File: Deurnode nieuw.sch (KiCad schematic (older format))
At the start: 34 parts, among them J1 EXT1, J12 Screw_Terminal_01x03, J14 Screw_Terminal_01x02, J15 Screw_Terminal_01x02, J18 BarrelJack_DC5.5F, J19 Jumper Use external 12V, J2 EXT2, J22 Force output Rel./FET on, J3 Conn_01x08, J4 Screw_Terminal_01x03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

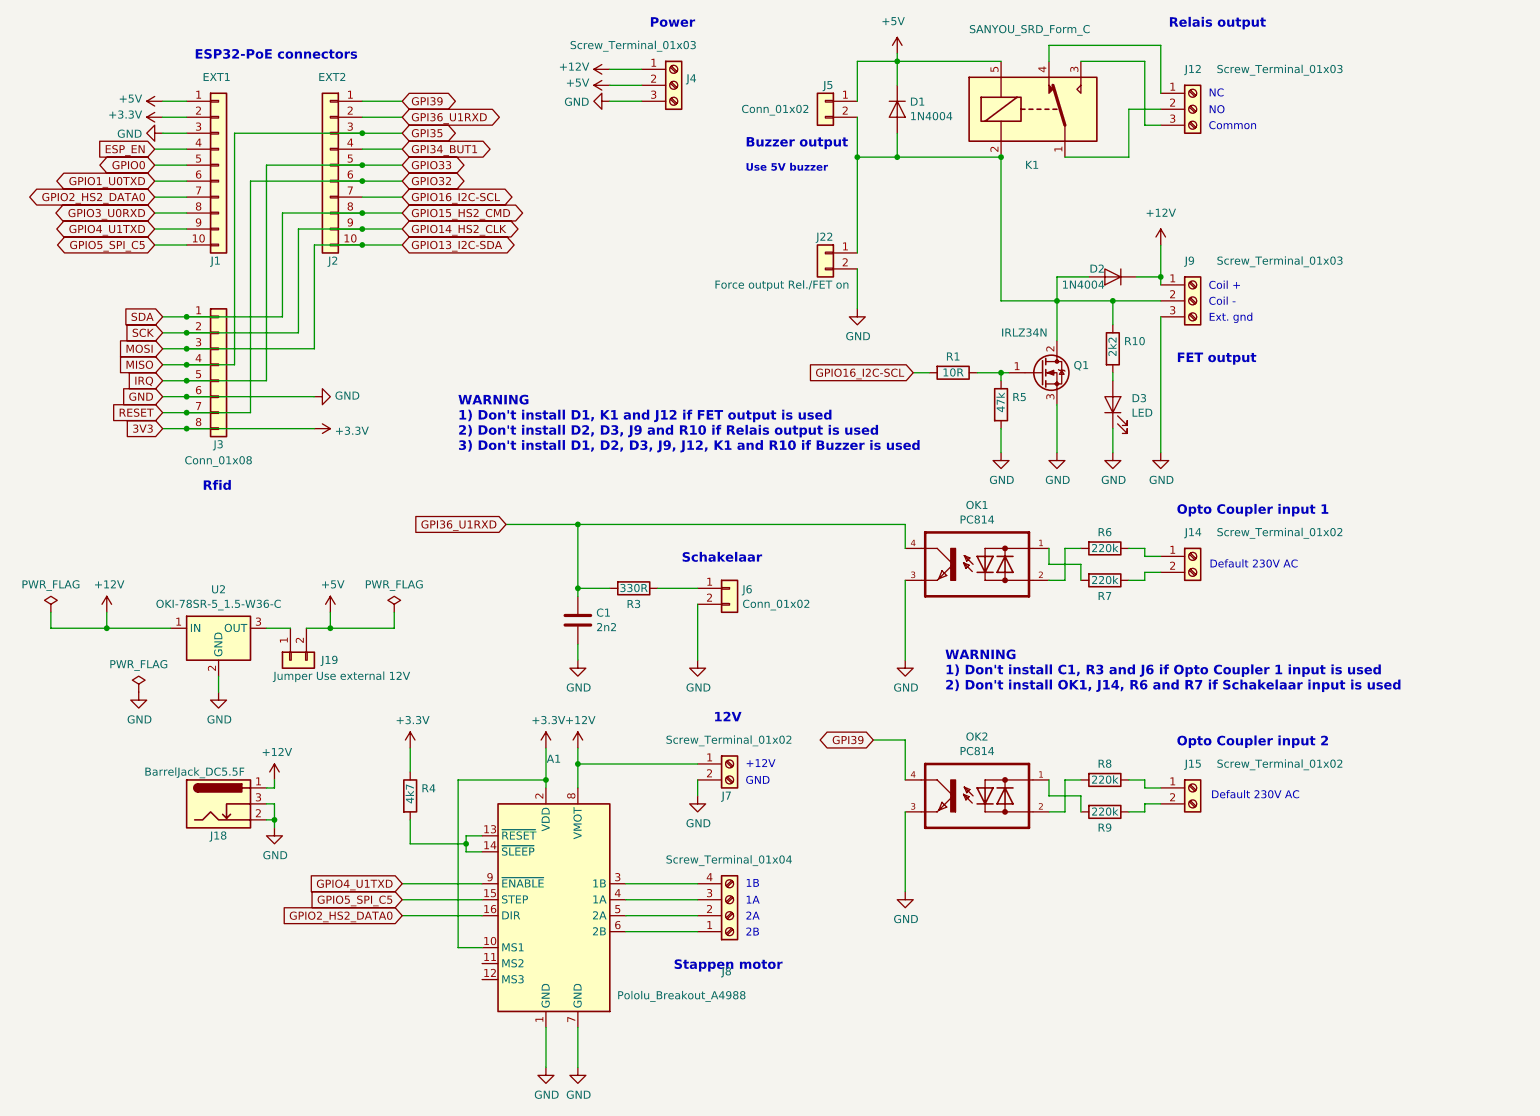
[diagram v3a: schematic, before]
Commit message: Relais and FET are controlled separately, buzzer resistor added. Current version Concep V0.8
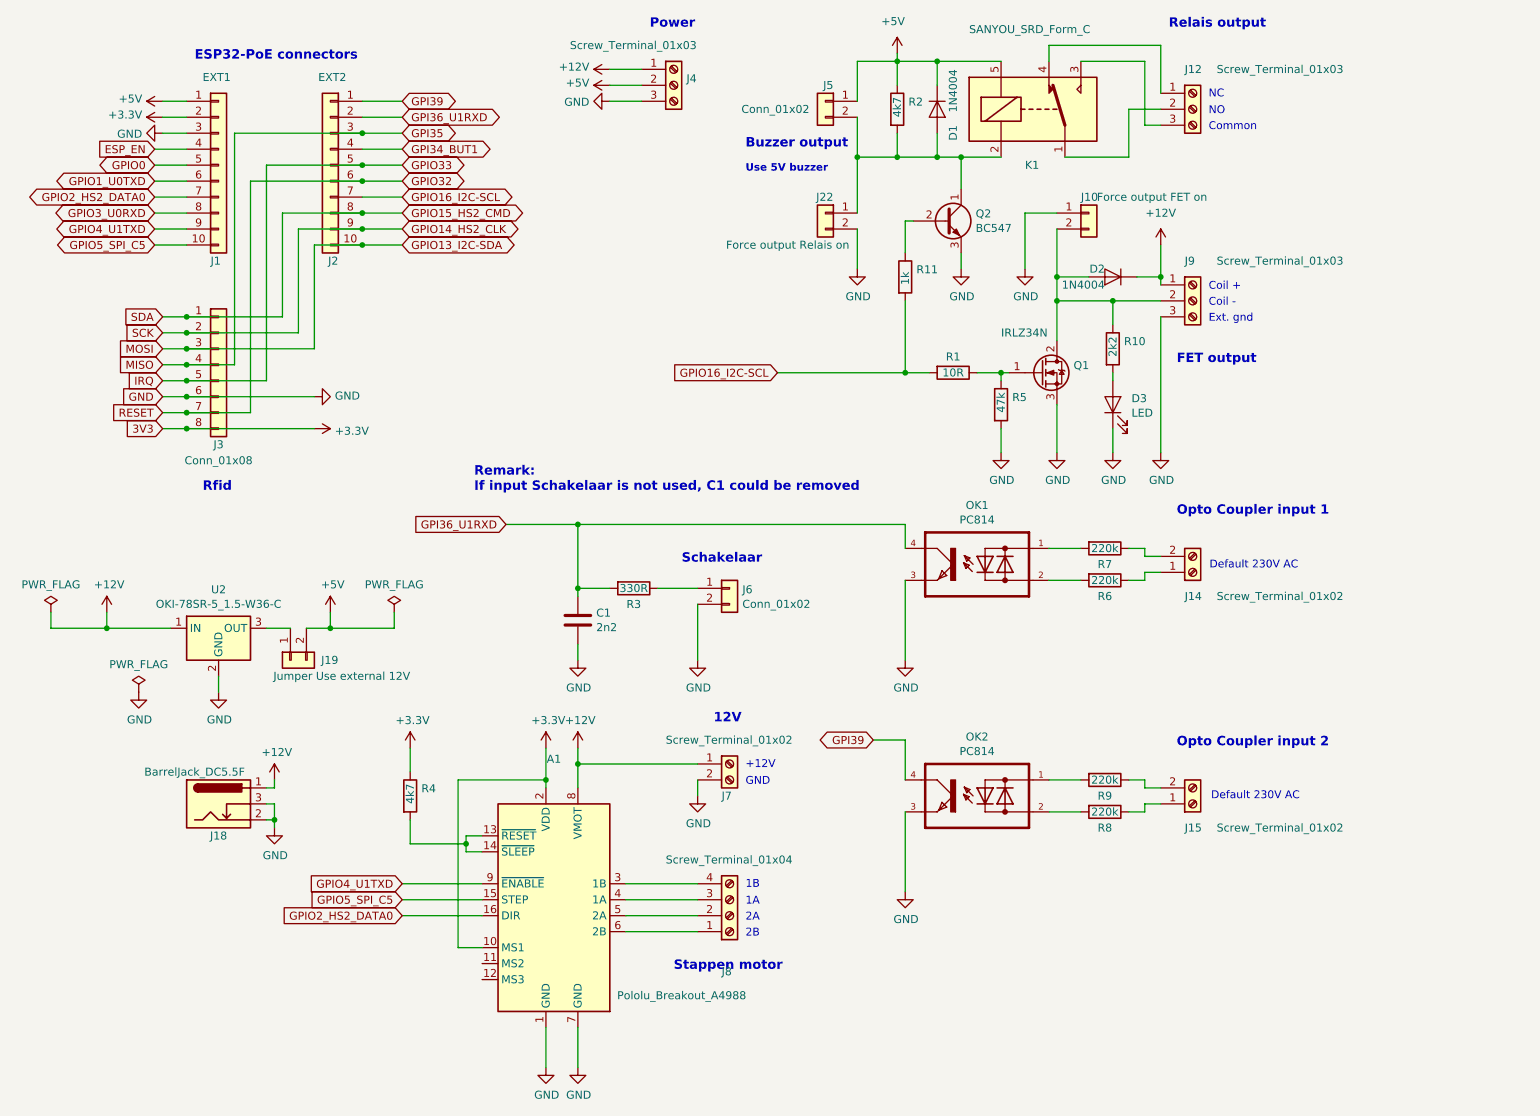
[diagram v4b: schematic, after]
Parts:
- added J10: Force output FET on, Connector_PinHeader_2.54mm:PinHeader_1x02_P2.54mm_Vertical, symbol Connector_Generic:Conn_01x02
- added Q2: BC547, Package_TO_SOT_THT:TO-92_Inline, symbol Transistor_BJT:BC547
- added R11: 1k, Resistor_THT:R_Axial_DIN0207_L6.3mm_D2.5mm_P7.62mm_Horizontal, symbol Device:R
- added R2: 4k7, Resistor_THT:R_Axial_DIN0207_L6.3mm_D2.5mm_P7.62mm_Horizontal, symbol Device:R
- J22: value Force output Rel./FET on -> Force output Relais on
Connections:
- net +5V: now also R2.1
- net GND: now also J10.1 (Pin_1), Q2.3 (E)
- net GPIO16_I2C-SCL: now also R11.2
- net at D1.2 (A), J22.1 (Pin_1), J5.2 (Pin_2)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: now also Q2.1 (C), R2.2; no longer D2.2 (A), J9.2 (Pin_2), Q1.2 (D), R10.1
- new net: D2.2 (A), J10.2 (Pin_2), J9.2 (Pin_2), Q1.2 (D), R10.1
- new net: Q2.2 (B), R11.1
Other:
- note added: "Remark:\nIf input Schakelaar is not used, C1 could be removed"
- note removed: "WARNING\n1) Don't install C1, R3 and J6 if Opto Coupler 1 input is used\n2) Don't install OK1, J14, R6 and R7 if Schakelaar input is used"
- note removed: "WARNING\n1) Don't install D1, K1 and J12 if FET output is used\n2) Don't install D2, D3, J9 and R10 if Relais output is used\n3) Don't install D1, D2, D3, J9, J12, K1 and R10 if Buzzer is used"
- moved on the sheet: D1, J22, R6, R7, R8, R9
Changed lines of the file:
@@
 Sheet 1 1
 Title "Deurnode (based on Olimex ESP32-POE)"
-Date "2020-03-07"
-Rev "Version 0.7"
+Date "2020-03-08"
+Rev "Version 0.8"
 Comp "Makerspace Leiden"
 Comment1 "Hans Beerman"
@@
 	0    1    1    0
 $EndComp
-Text GLabel 6850 2800 0    50   Input ~ 0
+Text GLabel 6000 2800 0    50   Input ~ 0
 GPIO16_I2C-SCL
 Wire Wire Line
@@
 Wire Wire Line
 	6750 1000 6750 850
-Wire Wire Line
-	6750 850  7400 850
 $Comp
 L power:+5V #PWR04
@@
 L Connector:Screw_Terminal_01x02 J14
 U 1 1 5E5F8709
-P 8600 3950
-F 0 "J14" H 8550 4100 50  0000 L CNN
-F 1 "Screw_Terminal_01x02" H 8750 4100 50  0000 L CNN
-F 2 "TerminalBlock_RND:TerminalBlock_RND_205-00287_1x02_P5.08mm_Horizontal" H 8600 3950 50  0001 C CNN
-F 3 "~" H 8600 3950 50  0001 C CNN
-	1    8600 3950
-	1    0    0    -1
+P 8600 4050
+F 0 "J14" H 8550 4200 50  0000 L CNN
+F 1 "Screw_Terminal_01x02" H 8750 4200 50  0000 L CNN
+F 2 "TerminalBlock_RND:TerminalBlock_RND_205-00287_1x02_P5.08mm_Horizontal" H 8600 4050 50  0001 C CNN
+F 3 "~" H 8600 4050 50  0001 C CNN
+	1    8600 4050
+	1    0    0    1
 $EndComp
 $Comp
 L Device:R R6
 U 1 1 5E5F9735
-P 8050 3900
-F 0 "R6" V 7950 3900 50  0000 C CNN
-F 1 "220k" V 8050 3900 50  0000 C CNN
-F 2 "Resistor_THT:R_Axial_DIN0207_L6.3mm_D2.5mm_P7.62mm_Horizontal" V 7980 3900 50  0001 C CNN
-F 3 "~" H 8050 3900 50  0001 C CNN
-	1    8050 3900
-	0    1    1    0
-$EndComp
-$Comp
-L Device:R R7
-U 1 1 5E5F9EE9
 P 8050 4100
-F 0 "R7" V 8150 4100 50  0000 C CNN
+F 0 "R6" V 8150 4100 50  0000 C CNN
 F 1 "220k" V 8050 4100 50  0000 C CNN
 F 2 "Resistor_THT:R_Axial_DIN0207_L6.3mm_D2.5mm_P7.62mm_Horizontal" V 7980 4100 50  0001 C CNN
@@
 L Connector:Screw_Terminal_01x02 J15
 U 1 1 5E676B21
-P 8600 5400
-F 0 "J15" H 8550 5550 50  0000 L CNN
-F 1 "Screw_Terminal_01x02" H 8750 5550 50  0000 L CNN
-F 2 "TerminalBlock_RND:TerminalBlock_RND_205-00287_1x02_P5.08mm_Horizontal" H 8600 5400 50  0001 C CNN
-F 3 "~" H 8600 5400 50  0001 C CNN
-	1    8600 5400
-	1    0    0    -1
+P 8600 5500
+F 0 "J15" H 8550 5650 50  0000 L CNN
+F 1 "Screw_Terminal_01x02" H 8750 5650 50  0000 L CNN
+F 2 "TerminalBlock_RND:TerminalBlock_RND_205-00287_1x02_P5.08mm_Horizontal" H 8600 5500 50  0001 C CNN
+F 3 "~" H 8600 5500 50  0001 C CNN
+	1    8600 5500
+	1    0    0    1
 $EndComp
 $Comp
 L Device:R R8
 U 1 1 5E676B27
+P 8050 5550
+F 0 "R8" V 8150 5550 50  0000 C CNN
+F 1 "220k" V 8050 5550 50  0000 C CNN
+F 2 "Resistor_THT:R_Axial_DIN0207_L6.3mm_D2.5mm_P7.62mm_Horizontal" V 7980 5550 50  0001 C CNN
+F 3 "~" H 8050 5550 50  0001 C CNN
+	1    8050 5550
+	0    1    1    0
+$EndComp
+$Comp
+L Device:R R9
+U 1 1 5E676B2D
 P 8050 5350
-F 0 "R8" V 7950 5350 50  0000 C CNN
+F 0 "R9" V 8150 5350 50  0000 C CNN
 F 1 "220k" V 8050 5350 50  0000 C CNN
 F 2 "Resistor_THT:R_Axial_DIN0207_L6.3mm_D2.5mm_P7.62mm_Horizontal" V 7980 5350 50  0001 C CNN
 F 3 "~" H 8050 5350 50  0001 C CNN
 	1    8050 5350
-	0    1    1    0
-$EndComp
-$Comp
-L Device:R R9
-U 1 1 5E676B2D
-P 8050 5550
-F 0 "R9" V 8150 5550 50  0000 C CNN
-F 1 "220k" V 8050 5550 50  0000 C CNN
-F 2 "Resistor_THT:R_Axial_DIN0207_L6.3mm_D2.5mm_P7.62mm_Horizontal" V 7980 5550 50  0001 C CNN
-F 3 "~" H 8050 5550 50  0001 C CNN
-	1    8050 5550
 	0    1    1    0
 $EndComp
@@
 Text Notes 8715 5480 0    49   ~ 0
 Default 230V AC
-Wire Wire Line
-	6950 2800 6850 2800
 $Comp
 L power:GND #PWR0110
 U 1 1 5E6923E9
-P 6500 2400
-F 0 "#PWR0110" H 6500 2150 50  0001 C CNN
-F 1 "GND" H 6505 2227 50  0000 C CNN
-F 2 "" H 6500 2400 50  0001 C CNN
-F 3 "" H 6500 2400 50  0001 C CNN
-	1    6500 2400
-	1    0    0    -1
-$EndComp
-Wire Wire Line
-	6500 2400 6500 2150
+P 6500 2150
+F 0 "#PWR0110" H 6500 1900 50  0001 C CNN
+F 1 "GND" H 6505 1977 50  0000 C CNN
+F 2 "" H 6500 2150 50  0001 C CNN
+F 3 "" H 6500 2150 50  0001 C CNN
+	1    6500 2150
+	1    0    0    -1
+$EndComp
+Wire Wire Line
+	6500 2150 6500 1900
 $Comp
 L Connector:Barrel_Jack_Switch J18
@@
 L Connector_Generic:Conn_01x02 J22
 U 1 1 5E6404FC
-P 6300 2050
-F 0 "J22" H 6250 2150 50  0000 L CNN
-F 1 "Force output Rel./FET on" H 6150 1850 50  0000 L CNN
-F 2 "Connector_PinHeader_2.54mm:PinHeader_1x02_P2.54mm_Vertical" H 6300 2050 50  0001 C CNN
-F 3 "~" H 6300 2050 50  0001 C CNN
-	1    6300 2050
+P 6300 1800
+F 0 "J22" H 6250 1900 50  0000 L CNN
+F 1 "Force output Relais on" H 6150 1600 50  0000 L CNN
+F 2 "Connector_PinHeader_2.54mm:PinHeader_1x02_P2.54mm_Vertical" H 6300 1800 50  0001 C CNN
+F 3 "~" H 6300 1800 50  0001 C CNN
+	1    6300 1800
 	-1   0    0    -1
 $EndComp
-Wire Wire Line
-	7400 1450 7400 2350
-Wire Wire Line
-	7400 2350 7750 2350
 $Comp
 L power:+12V #PWR016
@@
 Wire Wire Line
 	8400 2200 8400 2250
-Text Notes 4000 3300 0    59   ~ 12
-WARNING\n1) Don't install D1, K1 and J12 if FET output is used\n2) Don't install D2, D3, J9 and R10 if Relais output is used\n3) Don't install D1, D2, D3, J9, J12, K1 and R10 if Buzzer is used
 Wire Wire Line
 	7250 2800 7400 2800
@@
 L Diode:1N4004 D1
 U 1 1 5E593BB3
-P 6750 1150
-F 0 "D1" V 6704 1229 50  0000 L CNN
-F 1 "1N4004" V 6795 1229 50  0000 L CNN
-F 2 "Diode_THT:D_DO-41_SOD81_P10.16mm_Horizontal" H 6750 975 50  0001 C CNN
-F 3 "http://www.vishay.com/docs/88503/1n4001.pdf" H 6750 1150 50  0001 C CNN
-	1    6750 1150
+P 7000 1150
+F 0 "D1" H 7100 1250 50  0000 L CNN
+F 1 "1N4004" H 6750 1250 50  0000 L CNN
+F 2 "Diode_THT:D_DO-41_SOD81_P10.16mm_Horizontal" H 7000 975 50  0001 C CNN
+F 3 "http://www.vishay.com/docs/88503/1n4001.pdf" H 7000 1150 50  0001 C CNN
+	1    7000 1150
 	0    1    1    0
 $EndComp
@@
 Connection ~ 6750 1450
 Wire Wire Line
-	6750 1450 7400 1450
-Wire Wire Line
-	6500 2050 6500 1450
+	6500 1800 6500 1450
 Connection ~ 6500 1450
-Text Notes 7050 4800 0    59   ~ 12
-WARNING\n1) Don't install C1, R3 and J6 if Opto Coupler 1 input is used\n2) Don't install OK1, J14, R6 and R7 if Schakelaar input is used
+Text Notes 4100 3550 0    59   ~ 12
+Remark:\nIf input Schakelaar is not used, C1 could be removed
 Wire Wire Line
 	7800 1450 8200 1450
@@
 	1    0    0    -1
 $EndComp
-Connection ~ 7400 1450
-Wire Wire Line
-	7700 4100 7800 4100
-Wire Wire Line
-	7800 4100 7800 3900
-Wire Wire Line
-	7800 3900 7900 3900
-Wire Wire Line
-	7900 4100 7900 4000
-Wire Wire Line
-	7900 4000 7700 4000
-Wire Wire Line
-	7700 4000 7700 3900
-Wire Wire Line
-	7700 5350 7700 5450
-Wire Wire Line
-	7700 5450 7900 5450
-Wire Wire Line
-	7900 5450 7900 5550
-Wire Wire Line
-	7700 5550 7800 5550
-Wire Wire Line
-	7800 5550 7800 5350
-Wire Wire Line
-	7800 5350 7900 5350
+$Comp
+L Transistor_BJT:BC547 Q2
+U 1 1 5E6740A8
+P 7050 1850
+F 0 "Q2" H 7241 1896 50  0000 L CNN
+F 1 "BC547" H 7241 1805 50  0000 L CNN
+F 2 "Package_TO_SOT_THT:TO-92_Inline" H 7250 1775 50  0001 L CIN
+F 3 "http://www.fairchildsemi.com/ds/BC/BC547.pdf" H 7050 1850 50  0001 L CNN
+	1    7050 1850
+	1    0    0    -1
+$EndComp
+$Comp
+L power:GND #PWR011
+U 1 1 5E67C879
+P 7150 2150
+F 0 "#PWR011" H 7150 1900 50  0001 C CNN
+F 1 "GND" H 7155 1977 50  0000 C CNN
+F 2 "" H 7150 2150 50  0001 C CNN
+F 3 "" H 7150 2150 50  0001 C CNN
+	1    7150 2150
+	1    0    0    -1
+$EndComp
+Wire Wire Line
+	7150 2150 7150 2050
+Wire Wire Line
+	6950 2800 6800 2800
+$Comp
+L Device:R R11
+U 1 1 5E68BC49
+P 6800 2200
+F 0 "R11" H 6870 2246 50  0000 L CNN
+F 1 "1k" V 6800 2150 50  0000 L CNN
+F 2 "Resistor_THT:R_Axial_DIN0207_L6.3mm_D2.5mm_P7.62mm_Horizontal" V 6730 2200 50  0001 C CNN
+F 3 "~" H 6800 2200 50  0001 C CNN
+	1    6800 2200
+	1    0    0    -1
+$EndComp
+Wire Wire Line
+	6800 2350 6800 2800
+Connection ~ 6800 2800
+Wire Wire Line
+	6800 2800 6000 2800
+Wire Wire Line
+	6800 2050 6800 1850
+Wire Wire Line
+	6800 1850 6850 1850
+$Comp
+L Connector_Generic:Conn_01x02 J10
+U 1 1 5E6B22A0
+P 7950 1800
+F 0 "J10" H 7900 1900 50  0000 L CNN
+F 1 "Force output FET on" H 8000 1900 50  0000 L CNN
+F 2 "Connector_PinHeader_2.54mm:PinHeader_1x02_P2.54mm_Vertical" H 7950 1800 50  0001 C CNN
+F 3 "~" H 7950 1800 50  0001 C CNN
+	1    7950 1800
+	1    0    0    -1
+$EndComp
+Wire Wire Line
+	7150 1650 7150 1450
+Connection ~ 7150 1450
+Wire Wire Line
+	7150 1450 7400 1450
+Wire Wire Line
+	7750 1900 7750 2200
+Connection ~ 7750 2200
+$Comp
+L power:GND #PWR018
+U 1 1 5E6DA6A3
+P 7550 2150
+F 0 "#PWR018" H 7550 1900 50  0001 C CNN
+F 1 "GND" H 7555 1977 50  0000 C CNN
+F 2 "" H 7550 2150 50  0001 C CNN
+F 3 "" H 7550 2150 50  0001 C CNN
+	1    7550 2150
+	1    0    0    -1
+$EndComp
+Wire Wire Line
+	7550 2150 7550 1800
+Wire Wire Line
+	7550 1800 7750 1800
+Wire Wire Line
+	6750 850  7000 850
+Wire Wire Line
+	6750 1450 7000 1450
+Wire Wire Line
+	7000 1300 7000 1450
+Connection ~ 7000 1450
+Wire Wire Line
+	7000 1450 7150 1450
+Wire Wire Line
+	7000 1000 7000 850
+Connection ~ 7000 850
+Wire Wire Line
+	7000 850  7400 850
+$Comp
+L Device:R R2
+U 1 1 5E705D16
+P 6750 1150
+F 0 "R2" H 6820 1196 50  0000 L CNN
+F 1 "4k7" V 6750 1100 50  0000 L CNN
+F 2 "Resistor_THT:R_Axial_DIN0207_L6.3mm_D2.5mm_P7.62mm_Horizontal" V 6680 1150 50  0001 C CNN
+F 3 "~" H 6750 1150 50  0001 C CNN
+	1    6750 1150
+	1    0    0    -1
+$EndComp
+$Comp
+L Device:R R7
+U 1 1 5E5F9EE9
+P 8050 3900
+F 0 "R7" V 8150 3900 50  0000 C CNN
+F 1 "220k" V 8050 3900 50  0000 C CNN
+F 2 "Resistor_THT:R_Axial_DIN0207_L6.3mm_D2.5mm_P7.62mm_Horizontal" V 7980 3900 50  0001 C CNN
+F 3 "~" H 8050 3900 50  0001 C CNN
+	1    8050 3900
+	0    1    1    0
+$EndComp
+Wire Wire Line
+	7700 5550 7900 5550
+Wire Wire Line
+	7700 5350 7900 5350
+Wire Wire Line
+	7700 3900 7900 3900
+Wire Wire Line
+	7900 4100 7700 4100
 $EndSCHEMATC
